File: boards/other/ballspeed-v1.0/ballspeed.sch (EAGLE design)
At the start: 21 parts, among them U1 MPM3620GQV-P, U2 MCP3008SL

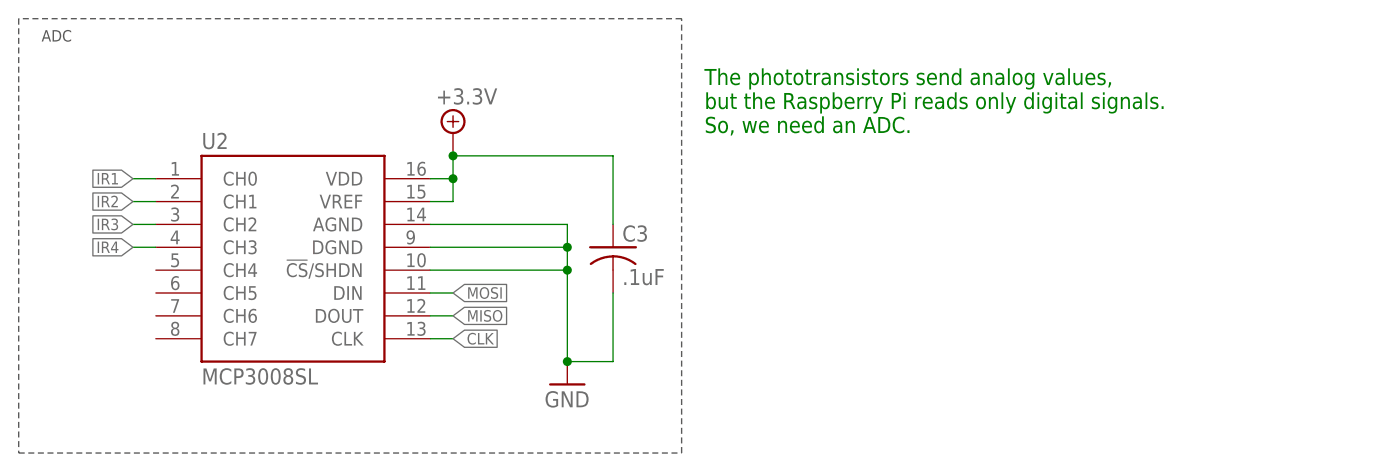
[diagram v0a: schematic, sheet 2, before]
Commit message: Adjusted ballspeed versioning
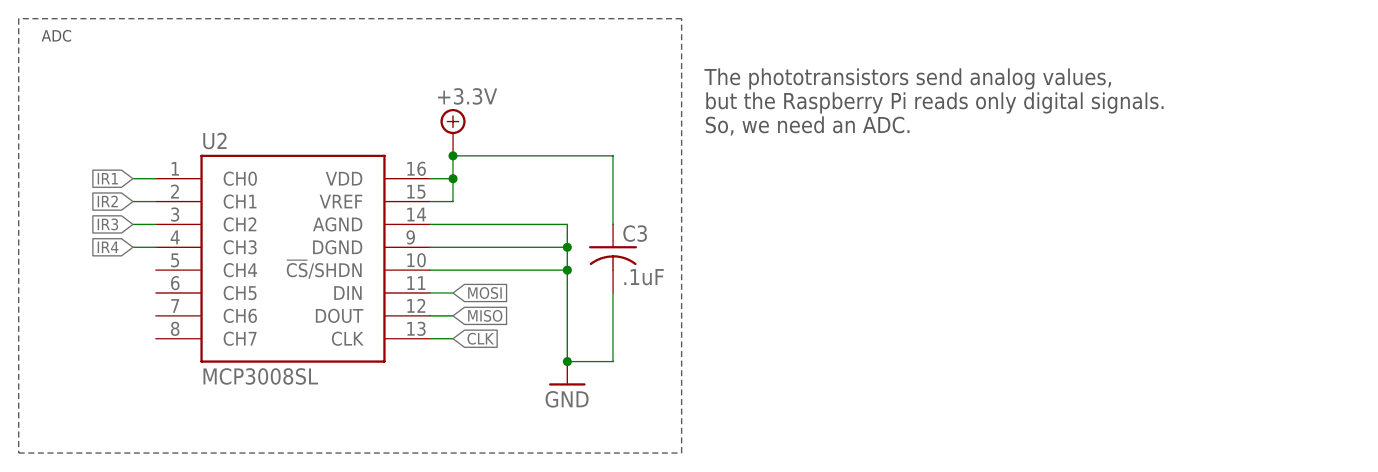
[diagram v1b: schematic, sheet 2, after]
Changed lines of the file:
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@@
 <?xml version="1.0" encoding="utf-8"?>
 <!DOCTYPE eagle SYSTEM "eagle.dtd">
-<eagle version="9.5.2">
+<eagle version="9.6.1">
 <drawing>
 <settings>
-<setting alwaysvectorfont="no"/>
+<setting alwaysvectorfont="yes"/>
 <setting verticaltext="up"/>
 </settings>
@@
 <attributes>
 <attribute name="REVISION" value="v1.0"/>
-<attribute name="TEAM" value="RoboCup"/>
+<attribute name="TEAM" value="RoboCup SSL"/>
 </attributes>
 <variantdefs>
@@
 <part name="SUPPLY4" library="RoboJackets-Supplies" deviceset="+3.3V" device=""/>
 <part name="FRAME1" library="RoboJackets-Frames" deviceset="FRAME_A_L" device="">
-<attribute name="REVISION" value=""/>
-<attribute name="TEAM" value=""/>
+<attribute name="REVISION" value="v1.0"/>
+<attribute name="SCH_DESC" value="Connectors"/>
+<attribute name="TEAM" value="RoboCup SSL"/>
 </part>
 <part name="FRAME2" library="RoboJackets-Frames" deviceset="FRAME_A_L" device="">
-<attribute name="REVISION" value=""/>
-<attribute name="TEAM" value=""/>
+<attribute name="REVISION" value="v1.0"/>
+<attribute name="SCH_DESC" value="ADC"/>
+<attribute name="TEAM" value="RoboCup SSL"/>
 </part>
 <part name="FRAME3" library="RoboJackets-Frames" deviceset="FRAME_A_L" device="">
-<attribute name="REVISION" value=""/>
-<attribute name="TEAM" value=""/>
+<attribute name="REVISION" value="v1.0"/>
+<attribute name="SCH_DESC" value="5V Regulator"/>
+<attribute name="TEAM" value="RoboCup SSL"/>
 </part>
 <part name="C3" library="rcl" library_urn="urn:adsk.eagle:library:334" deviceset="C-US" device="C0603" package3d_urn="urn:adsk.eagle:package:23616/2" value=".1uF"/>
@@
 <attribute name="TEAM" x="163.83" y="-95.25" size="3.048" layer="94" ratio="10" align="top-left"/>
 <attribute name="REVISION" x="234.95" y="-123.19" size="2.54" layer="94"/>
+<attribute name="SCH_DESC" x="163.83" y="-123.19" size="2.54" layer="94"/>
 </instance>
 </instances>
@@
 <wire x1="0" y1="48.26" x2="0" y2="0" width="0.1524" layer="97" style="longdash"/>
 <text x="2.54" y="45.72" size="1.27" layer="97">ADC</text>
-<text x="76.2" y="35.56" size="1.778" layer="91">The phototransistors send analog values,
+<text x="76.2" y="35.56" size="1.778" layer="97">The phototransistors send analog values,
 but the Raspberry Pi reads only digital signals.
 So, we need an ADC.</text>
@@
 <attribute name="TEAM" x="163.83" y="-123.19" size="3.048" layer="94" ratio="10" align="top-left"/>
 <attribute name="REVISION" x="234.95" y="-151.13" size="2.54" layer="94"/>
+<attribute name="SCH_DESC" x="163.83" y="-151.13" size="2.54" layer="94"/>
 </instance>
 <instance part="C3" gate="G$1" x="66.04" y="22.86" smashed="yes">
@@
 <attribute name="TEAM" x="161.29" y="-87.63" size="3.048" layer="94" ratio="10" align="top-left"/>
 <attribute name="REVISION" x="232.41" y="-115.57" size="2.54" layer="94"/>
+<attribute name="SCH_DESC" x="161.29" y="-115.57" size="2.54" layer="94"/>
 </instance>
 </instances>
